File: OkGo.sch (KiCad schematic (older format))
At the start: 7 parts

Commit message: Finished first rev of schematic
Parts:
- added K? (x4): CONN_3, symbol CONN_3
- added SW? (x2): SW_PUSH, symbol SW_PUSH
- added SW? (x2): SPST, symbol SPST
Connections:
- wire segments 4 -> 38
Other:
- moved on the sheet: BT?, K?, P?, R?
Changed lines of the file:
@@
-EESchema Schematic File Version 2  date 25/11/2012 13:21:58
+EESchema Schematic File Version 2  date 25/11/2012 13:41:50
 LIBS:power
 LIBS:device
@@
 Comment4 ""
 $EndDescr
-Text Notes 550  4750 0    60   ~ 0
+Wire Notes Line
+	7200 3200 7200 4300
+Wire Notes Line
+	7200 3200 9300 3200
+Wire Notes Line
+	9300 3200 9300 4300
+Wire Notes Line
+	9300 4300 7200 4300
+Wire Wire Line
+	4000 2000 4000 5600
+Wire Wire Line
+	9100 4100 9100 3700
+Wire Wire Line
+	9100 3700 9000 3700
+Wire Wire Line
+	7650 3700 8400 3700
+Wire Wire Line
+	8400 3400 7900 3400
+Wire Wire Line
+	7900 3400 7900 3600
+Wire Wire Line
+	7900 3600 7650 3600
+Wire Wire Line
+	6700 3700 5500 3700
+Connection ~ 3800 5000
+Wire Wire Line
+	2800 5000 3800 5000
+Wire Wire Line
+	3800 2000 3800 2050
+Wire Wire Line
+	4550 3700 4300 3700
+Wire Wire Line
+	4300 3700 4300 4800
+Wire Wire Line
+	4300 4800 2800 4800
+Connection ~ 1500 5600
+Wire Wire Line
+	1500 5400 1500 5600
+Wire Wire Line
+	1500 4900 2000 4900
+Connection ~ 3800 4700
+Connection ~ 3800 3300
+Wire Wire Line
+	3800 4700 2800 4700
+Wire Wire Line
+	3800 1050 3600 1050
+Wire Wire Line
+	3600 1050 3600 750
+Wire Wire Line
+	4200 750  4200 1050
+Wire Wire Line
+	4200 1050 4000 1050
+Wire Wire Line
+	3800 3300 2800 3300
+Wire Wire Line
+	2800 3600 3800 3600
+Connection ~ 3800 3600
+Wire Wire Line
+	2000 3500 950  3500
+Wire Wire Line
+	950  4000 950  5600
+Wire Wire Line
+	2800 3400 4300 3400
+Wire Wire Line
+	4300 3400 4300 3600
+Wire Wire Line
+	4300 3600 4550 3600
+Wire Wire Line
+	950  5600 4550 5600
+Wire Wire Line
+	4550 5600 4550 3800
+Connection ~ 4000 5600
+Wire Wire Line
+	3800 3050 3800 5600
+Connection ~ 3800 5600
+Wire Wire Line
+	5500 3600 6700 3600
+Wire Wire Line
+	5500 3800 6700 3800
+Wire Wire Line
+	7650 3800 7900 3800
+Wire Wire Line
+	7900 3800 7900 4100
+Wire Wire Line
+	7900 4100 8000 4100
+Wire Wire Line
+	9000 3400 9200 3400
+Wire Wire Line
+	9200 3400 9200 4100
+Wire Wire Line
+	9200 4100 9000 4100
+Connection ~ 9100 4100
+Wire Notes Line
+	5000 5900 5000 1550
+Wire Notes Line
+	5000 5900 600  5900
+Wire Notes Line
+	600  5900 600  1550
+Wire Notes Line
+	600  1550 5000 1550
+$Comp
+L CONN_3 K?
+U 1 1 50B21F60
+P 7300 3700
+F 0 "K?" V 7250 3700 50  0000 C CNN
+F 1 "CONN_3" V 7350 3700 40  0000 C CNN
+	1    7300 3700
+	-1   0    0    1
+$EndComp
+$Comp
+L CONN_3 K?
+U 1 1 50B21F5E
+P 7050 3700
+F 0 "K?" V 7000 3700 50  0000 C CNN
+F 1 "CONN_3" V 7100 3700 40  0000 C CNN
+	1    7050 3700
+	1    0    0    1
+$EndComp
+$Comp
+L SPST SW?
+U 1 1 50B21E62
+P 8500 4100
+F 0 "SW?" H 8500 4200 70  0000 C CNN
+F 1 "SPST" H 8500 4000 70  0000 C CNN
+	1    8500 4100
+	1    0    0    -1
+$EndComp
+$Comp
+L SPST SW?
+U 1 1 50B21E5F
+P 3800 2550
+F 0 "SW?" H 3800 2650 70  0000 C CNN
+F 1 "SPST" H 3800 2450 70  0000 C CNN
+	1    3800 2550
+	0    -1   -1   0
+$EndComp
+$Comp
+L SW_PUSH SW?
+U 1 1 50B21E58
+P 8700 3700
+F 0 "SW?" H 8850 3810 50  0000 C CNN
+F 1 "SW_PUSH" H 8700 3620 50  0000 C CNN
+	1    8700 3700
+	1    0    0    -1
+$EndComp
+$Comp
+L SW_PUSH SW?
+U 1 1 50B21E55
+P 8700 3400
+F 0 "SW?" H 8850 3510 50  0000 C CNN
+F 1 "SW_PUSH" H 8700 3320 50  0000 C CNN
+	1    8700 3400
+	1    0    0    -1
+$EndComp
+$Comp
+L CONN_3 K?
+U 1 1 50B21DFA
+P 5150 3700
+F 0 "K?" V 5100 3700 50  0000 C CNN
+F 1 "CONN_3" V 5200 3700 40  0000 C CNN
+	1    5150 3700
+	-1   0    0    1
+$EndComp
+$Comp
+L CONN_3 K?
+U 1 1 50B21DF6
+P 4900 3700
+F 0 "K?" V 4850 3700 50  0000 C CNN
+F 1 "CONN_3" V 4950 3700 40  0000 C CNN
+	1    4900 3700
+	1    0    0    1
+$EndComp
+Text Notes 1050 5150 0    60   ~ 0
 IGNITION
-Text Notes 700  3550 0    60   ~ 0
+Text Notes 650  3750 0    60   ~ 0
 OXID\nVALVE
 $Comp
 L R R?
 U 1 1 50B219E4
-P 1000 4750
-F 0 "R?" V 1080 4750 50  0000 C CNN
-F 1 "R" V 1000 4750 50  0000 C CNN
-	1    1000 4750
+P 1500 5150
+F 0 "R?" V 1580 5150 50  0000 C CNN
+F 1 "R" V 1500 5150 50  0000 C CNN
+	1    1500 5150
 	1    0    0    -1
 $EndComp
@@
 L R R?
 U 1 1 50B219DE
-P 1000 3550
-F 0 "R?" V 1080 3550 50  0000 C CNN
-F 1 "R" V 1000 3550 50  0000 C CNN
-	1    1000 3550
+P 950 3750
+F 0 "R?" V 1030 3750 50  0000 C CNN
+F 1 "R" V 950 3750 50  0000 C CNN
+	1    950  3750
 	1    0    0    -1
 $EndComp
@@
 L RELAY_2RT K?
 U 1 1 50B219CD
-P 2400 4850
-F 0 "K?" H 2350 5250 70  0000 C CNN
-F 1 "RELAY_2RT" H 2550 4350 70  0000 C CNN
-	1    2400 4850
-	1    0    0    -1
+P 2400 5050
+F 0 "K?" H 2350 5450 70  0000 C CNN
+F 1 "RELAY_2RT" H 2550 4550 70  0000 C CNN
+	1    2400 5050
+	-1   0    0    1
 $EndComp
 $Comp
 L RELAY_2RT K?
 U 1 1 50B219C6
-P 2400 3600
-F 0 "K?" H 2350 4000 70  0000 C CNN
-F 1 "RELAY_2RT" H 2550 3100 70  0000 C CNN
-	1    2400 3600
-	1    0    0    -1
-$EndComp
-Wire Wire Line
-	4050 2700 4250 2700
-Wire Wire Line
-	4250 2700 4250 2400
-Wire Wire Line
-	3650 2400 3650 2700
-Wire Wire Line
-	3650 2700 3850 2700
+P 2400 3650
+F 0 "K?" H 2350 4050 70  0000 C CNN
+F 1 "RELAY_2RT" H 2550 3150 70  0000 C CNN
+	1    2400 3650
+	-1   0    0    1
+$EndComp
 $Comp
 L CONN_2 P?
 U 1 1 50B21968
-P 3950 3300
-F 0 "P?" V 3900 3300 40  0000 C CNN
-F 1 "CONN_2" V 4000 3300 40  0000 C CNN
-	1    3950 3300
+P 3900 1650
+F 0 "P?" V 3850 1650 40  0000 C CNN
+F 1 "CONN_2" V 3950 1650 40  0000 C CNN
+	1    3900 1650
 	0    1    -1   0
 $EndComp
@@
 L CONN_2 P?
 U 1 1 50B21962
-P 3950 3050
-F 0 "P?" V 3900 3050 40  0000 C CNN
-F 1 "CONN_2" V 4000 3050 40  0000 C CNN
-	1    3950 3050
+P 3900 1400
+F 0 "P?" V 3850 1400 40  0000 C CNN
+F 1 "CONN_2" V 3950 1400 40  0000 C CNN
+	1    3900 1400
 	0    1    1    0
 $EndComp
@@
 L BATTERY BT?
 U 1 1 50B2192F
-P 3950 2400
-F 0 "BT?" H 3950 2600 50  0000 C CNN
-F 1 "BATTERY" H 3950 2210 50  0000 C CNN
-	1    3950 2400
-	1    0    0    -1
-$EndComp
+P 3900 750
+F 0 "BT?" H 3900 950 50  0000 C CNN
+F 1 "BATTERY" H 3900 560 50  0000 C CNN
+	1    3900 750
+	1    0    0    -1
+$EndComp

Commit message: Added connectors on firing/oxid loads
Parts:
- added P? (x4): CONN_2, symbol CONN_2
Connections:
- wire segments 38 -> 49
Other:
- moved on the sheet: BT?, K?, P?, R?, SW?

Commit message: Added test and armed LEDs
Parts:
- removed K? (x4): CONN_3, symbol CONN_3
- added D? (x3): LED, symbol LED
- added P? (x4): CONN_4, symbol CONN_4
- added R? (x3): R, symbol R
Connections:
- wire segments 49 -> 62
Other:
- moved on the sheet: P?, R?

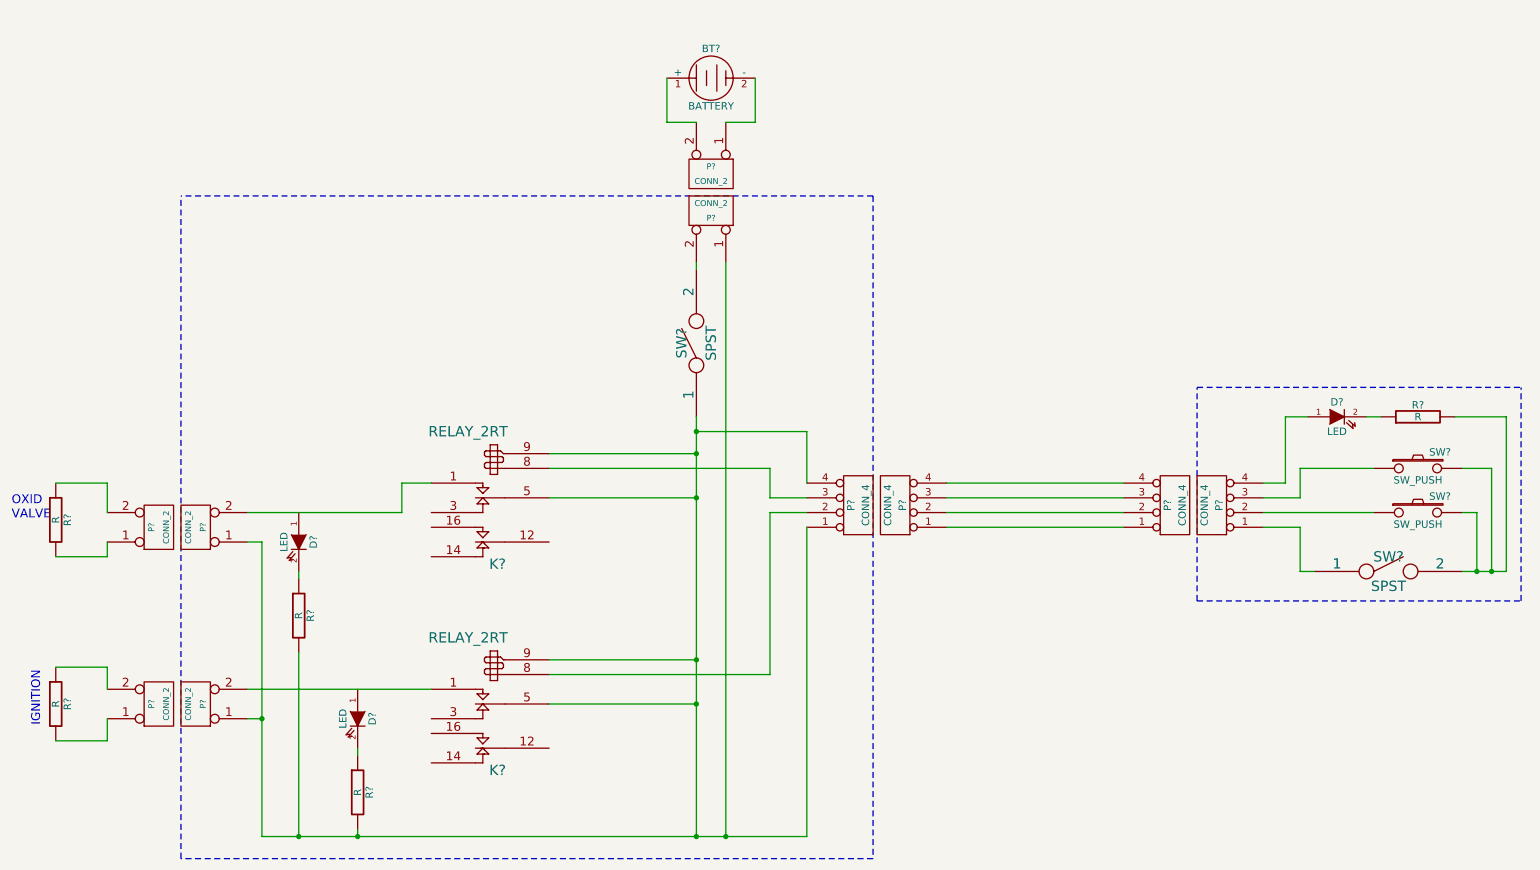
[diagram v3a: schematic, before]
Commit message: Added firing box armed LED
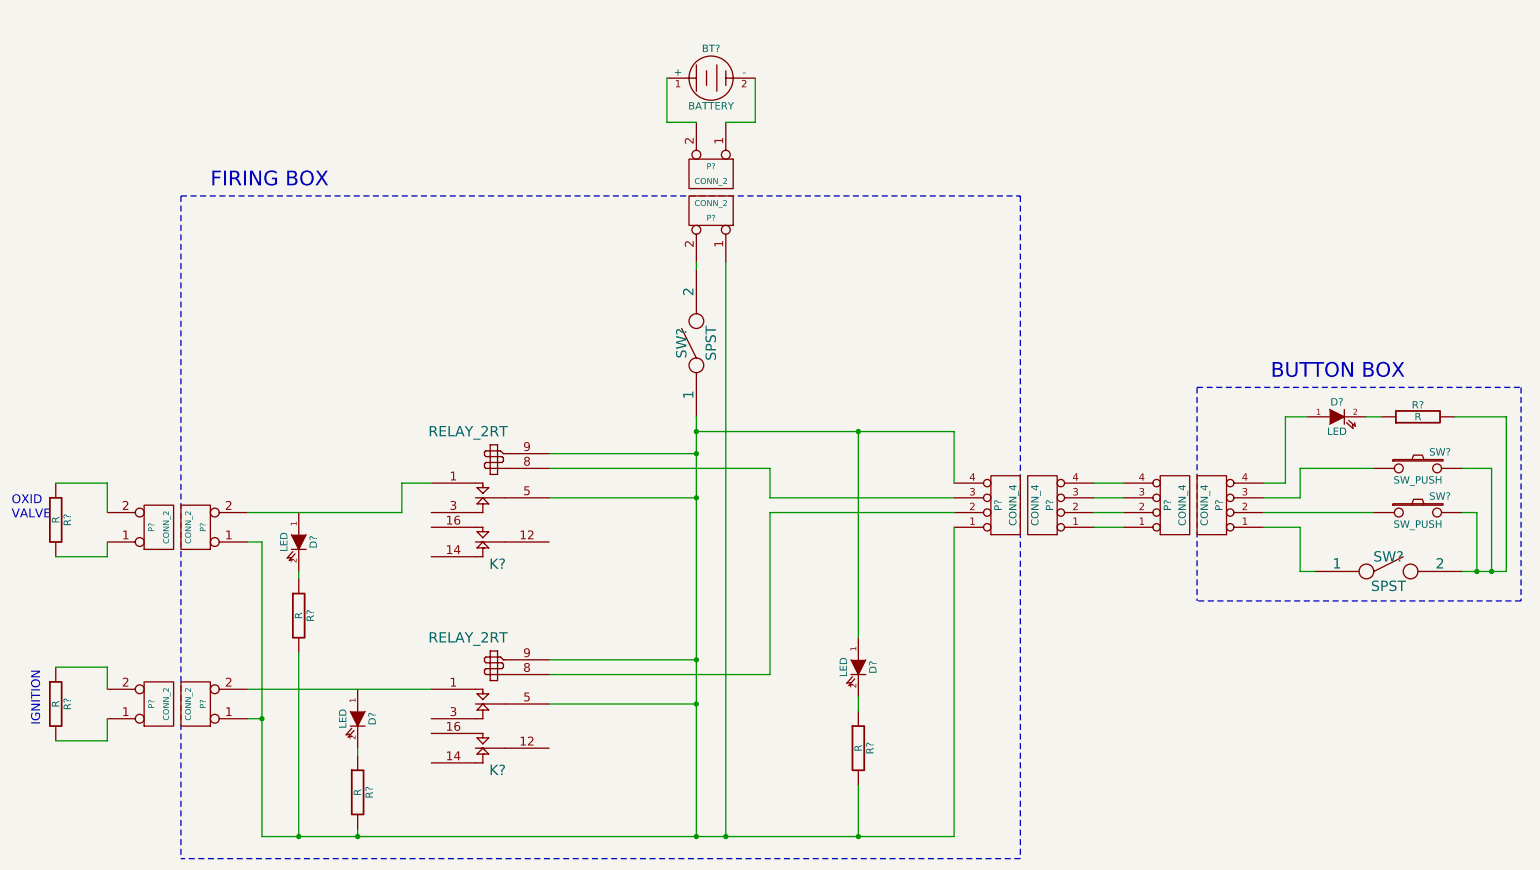
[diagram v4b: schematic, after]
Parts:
- added D?: LED, symbol LED
- added R?: R, symbol R
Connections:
- net at K?.5 (C1), K?.5 (C1), K?.9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: now also D?.1 (A), R?.2
- new net: D?.2 (K), R?.1
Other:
- note added: "BUTTON BOX"
- note added: "FIRING BOX"
- moved on the sheet: P?
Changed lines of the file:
@@
-EESchema Schematic File Version 2  date 25/11/2012 13:55:21
+EESchema Schematic File Version 2  date 25/11/2012 14:01:06
 LIBS:power
 LIBS:device
@@
 Comment4 ""
 $EndDescr
-Wire Notes Line
-	8600 4400 10800 4400
-Wire Notes Line
-	10800 4400 10800 2950
+Connection ~ 6300 6000
+Wire Wire Line
+	6300 5650 6300 6000
+Connection ~ 6300 3250
+Wire Wire Line
+	6300 4650 6300 3250
+Wire Notes Line
+	1700 1650 7400 1650
+Wire Wire Line
+	5200 3250 6950 3250
+Wire Wire Line
+	6950 3800 5700 3800
+Wire Wire Line
+	7900 3800 8100 3800
+Wire Wire Line
+	7900 3600 8100 3600
+Connection ~ 10600 4200
+Wire Wire Line
+	10400 4200 10700 4200
+Wire Wire Line
+	10700 4200 10700 3150
+Wire Wire Line
+	10700 3150 10350 3150
+Wire Wire Line
+	9350 3150 9200 3150
+Wire Wire Line
+	9200 3150 9200 3600
+Wire Wire Line
+	9200 3600 9050 3600
+Connection ~ 5200 3250
+Wire Wire Line
+	6950 3250 6950 3600
+Wire Notes Line
+	1700 1650 1700 6150
+Wire Notes Line
+	7400 1650 7400 6150
+Wire Wire Line
+	2900 5400 2900 5450
+Connection ~ 2900 6000
+Wire Wire Line
+	2900 5950 2900 6000
+Connection ~ 5400 6000
+Wire Wire Line
+	5400 6000 5400 2100
+Connection ~ 2250 5200
+Wire Wire Line
+	2150 5000 3400 5000
+Wire Wire Line
+	1200 5200 1200 5350
+Wire Wire Line
+	1200 5350 850  5350
+Wire Wire Line
+	1200 3800 1200 3600
+Wire Wire Line
+	1200 3600 850  3600
+Connection ~ 10500 4200
+Wire Wire Line
+	10600 4200 10600 3500
+Wire Wire Line
+	10600 3500 10400 3500
+Wire Wire Line
+	9400 4200 9300 4200
+Wire Wire Line
+	9300 4200 9300 3900
+Wire Wire Line
+	9300 3900 9050 3900
+Wire Wire Line
+	5700 3500 5700 3700
+Wire Wire Line
+	5700 3500 4200 3500
+Connection ~ 5200 3700
+Wire Wire Line
+	4200 3700 5200 3700
+Wire Wire Line
+	5200 3400 4200 3400
+Wire Wire Line
+	5400 1150 5600 1150
+Wire Wire Line
+	5600 1150 5600 850
+Wire Wire Line
+	5000 850  5000 1150
+Wire Wire Line
+	5000 1150 5200 1150
+Wire Wire Line
+	5200 4800 4200 4800
+Connection ~ 5200 3400
+Connection ~ 5200 4800
+Wire Wire Line
+	4200 4900 5700 4900
+Wire Wire Line
+	5700 4900 5700 3800
+Wire Wire Line
+	5200 2100 5200 2150
+Wire Wire Line
+	4200 5100 5200 5100
+Connection ~ 5200 5100
+Wire Wire Line
+	9050 3700 9300 3700
+Wire Wire Line
+	9300 3700 9300 3500
+Wire Wire Line
+	9300 3500 9800 3500
+Wire Wire Line
+	9050 3800 9800 3800
+Wire Wire Line
+	10400 3800 10500 3800
+Wire Wire Line
+	10500 3800 10500 4200
+Wire Wire Line
+	850  4100 1200 4100
+Wire Wire Line
+	1200 4100 1200 4000
+Wire Wire Line
+	3200 3600 3200 3800
+Wire Wire Line
+	3200 3600 3400 3600
+Wire Wire Line
+	850  4850 1200 4850
+Wire Wire Line
+	1200 4850 1200 5000
+Wire Wire Line
+	3200 3800 2150 3800
+Wire Wire Line
+	2150 4000 2250 4000
+Wire Wire Line
+	2250 5200 2150 5200
+Wire Wire Line
+	2250 4000 2250 6000
+Wire Wire Line
+	6950 3900 6950 6000
+Wire Wire Line
+	5200 6000 5200 3150
+Connection ~ 5200 6000
+Wire Wire Line
+	2500 4750 2500 6000
+Connection ~ 2500 6000
+Wire Wire Line
+	2500 4200 2500 4250
+Wire Wire Line
+	9750 3150 9850 3150
+Wire Notes Line
+	8600 2950 8600 4400
 Wire Notes Line
 	8600 2950 10800 2950
 Wire Notes Line
-	8600 4400 8600 2950
-Wire Wire Line
-	9750 3150 9850 3150
-Wire Wire Line
-	6900 3600 8100 3600
-Wire Notes Line
-	6400 1650 1700 1650
-Wire Wire Line
-	2500 4200 2500 4250
-Connection ~ 2500 6000
-Wire Wire Line
-	2500 4750 2500 6000
-Connection ~ 5200 6000
-Wire Wire Line
-	5200 6000 5200 3150
-Wire Wire Line
-	5950 3900 5950 6000
-Wire Wire Line
-	5950 6000 2250 6000
-Wire Wire Line
-	2250 6000 2250 4000
-Wire Wire Line
-	2250 5200 2150 5200
-Wire Wire Line
-	2250 4000 2150 4000
-Wire Wire Line
-	2150 3800 3200 3800
-Wire Wire Line
-	1200 5000 1200 4850
-Wire Wire Line
-	1200 4850 850  4850
-Wire Wire Line
-	3400 3600 3200 3600
-Wire Wire Line
-	3200 3600 3200 3800
-Wire Wire Line
-	1200 4000 1200 4100
-Wire Wire Line
-	1200 4100 850  4100
-Wire Wire Line
-	10500 4200 10500 3800
-Wire Wire Line
-	10500 3800 10400 3800
-Wire Wire Line
-	9050 3800 9800 3800
-Wire Wire Line
-	9800 3500 9300 3500
-Wire Wire Line
-	9300 3500 9300 3700
-Wire Wire Line
-	9300 3700 9050 3700
-Wire Wire Line
-	8100 3800 6900 3800
-Connection ~ 5200 5100
-Wire Wire Line
-	4200 5100 5200 5100
-Wire Wire Line
-	5200 2100 5200 2150
-Wire Wire Line
-	5950 3800 5700 3800
-Wire Wire Line
-	5700 3800 5700 4900
-Wire Wire Line
-	5700 4900 4200 4900
-Connection ~ 5200 4800
-Connection ~ 5200 3400
-Wire Wire Line
-	5200 4800 4200 4800
-Wire Wire Line
-	5200 1150 5000 1150
-Wire Wire Line
-	5000 1150 5000 850
-Wire Wire Line
-	5600 850  5600 1150
-Wire Wire Line
-	5600 1150 5400 1150
-Wire Wire Line
-	5200 3400 4200 3400
-Wire Wire Line
-	4200 3700 5200 3700
-Connection ~ 5200 3700
-Wire Wire Line
-	4200 3500 5700 3500
-Wire Wire Line
-	5700 3500 5700 3700
-Wire Wire Line
-	5700 3700 5950 3700
-Wire Wire Line
-	6900 3700 8100 3700
-Wire Wire Line
-	6900 3900 8100 3900
-Wire Wire Line
-	9050 3900 9300 3900
-Wire Wire Line
-	9300 3900 9300 4200
-Wire Wire Line
-	9300 4200 9400 4200
-Wire Wire Line
-	10400 3500 10600 3500
-Wire Wire Line
-	10600 3500 10600 4200
-Connection ~ 10500 4200
-Wire Wire Line
-	850  3600 1200 3600
-Wire Wire Line
-	1200 3600 1200 3800
-Wire Wire Line
-	850  5350 1200 5350
-Wire Wire Line
-	1200 5350 1200 5200
-Wire Wire Line
-	2150 5000 3400 5000
-Connection ~ 2250 5200
-Wire Wire Line
-	5400 6000 5400 2100
-Connection ~ 5400 6000
-Wire Wire Line
-	2900 5950 2900 6000
-Connection ~ 2900 6000
-Wire Wire Line
-	2900 5400 2900 5450
-Wire Notes Line
-	6400 1650 6400 6150
-Wire Notes Line
-	6400 6150 1700 6150
-Wire Notes Line
-	1700 6150 1700 1650
-Wire Wire Line
-	5200 3250 5950 3250
-Wire Wire Line
-	5950 3250 5950 3600
-Connection ~ 5200 3250
-Wire Wire Line
-	9050 3600 9200 3600
-Wire Wire Line
-	9200 3600 9200 3150
-Wire Wire Line
-	9200 3150 9350 3150
-Wire Wire Line
-	10350 3150 10700 3150
-Wire Wire Line
-	10700 3150 10700 4200
-Wire Wire Line
-	10700 4200 10400 4200
-Connection ~ 10600 4200
+	10800 2950 10800 4400
+Wire Notes Line
+	10800 4400 8600 4400
+Wire Wire Line
+	8100 3700 7900 3700
+Wire Wire Line
+	8100 3900 7900 3900
+Wire Wire Line
+	5700 3700 6950 3700
+Wire Wire Line
+	6950 6000 2250 6000
+Wire Notes Line
+	7400 6150 1700 6150
+Wire Wire Line
+	6300 5050 6300 5150
+$Comp
+L LED D?
+U 1 1 50B2244A
+P 6300 4850
+F 0 "D?" H 6300 4950 50  0000 C CNN
+F 1 "LED" H 6300 4750 50  0000 C CNN
+	1    6300 4850
+	0    1    1    0
+$EndComp
+$Comp
+L R R?
+U 1 1 50B22446
+P 6300 5400
+F 0 "R?" V 6380 5400 50  0000 C CNN
+F 1 "R" V 6300 5400 50  0000 C CNN
+	1    6300 5400
+	1    0    0    -1
+$EndComp
+Text Notes 9100 2900 0    100  ~ 0
+BUTTON BOX
+Text Notes 1900 1600 0    100  ~ 0
+FIRING BOX
 $Comp
 L R R?
@@
 L CONN_4 P?
 U 1 1 50B22307
-P 6550 3750
-F 0 "P?" V 6500 3750 50  0000 C CNN
-F 1 "CONN_4" V 6600 3750 50  0000 C CNN
-	1    6550 3750
+P 7550 3750
+F 0 "P?" V 7500 3750 50  0000 C CNN
+F 1 "CONN_4" V 7600 3750 50  0000 C CNN
+	1    7550 3750
 	-1   0    0    1
 $EndComp
@@
 L CONN_4 P?
 U 1 1 50B222FE
-P 6300 3750
-F 0 "P?" V 6250 3750 50  0000 C CNN
-F 1 "CONN_4" V 6350 3750 50  0000 C CNN
-	1    6300 3750
+P 7300 3750
+F 0 "P?" V 7250 3750 50  0000 C CNN
+F 1 "CONN_4" V 7350 3750 50  0000 C CNN
+	1    7300 3750
 	1    0    0    1
 $EndComp
